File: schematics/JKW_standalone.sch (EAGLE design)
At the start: 225 parts, among them IC1 4093D, IC4 ATMEGA2560-16AU, Q1 BSS84, Q10 BSS84, Q11 BSS84, Q2 BSS84, Q3 BSS84, Q4 BSS84, Q5 BSS84, Q6 BSS84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

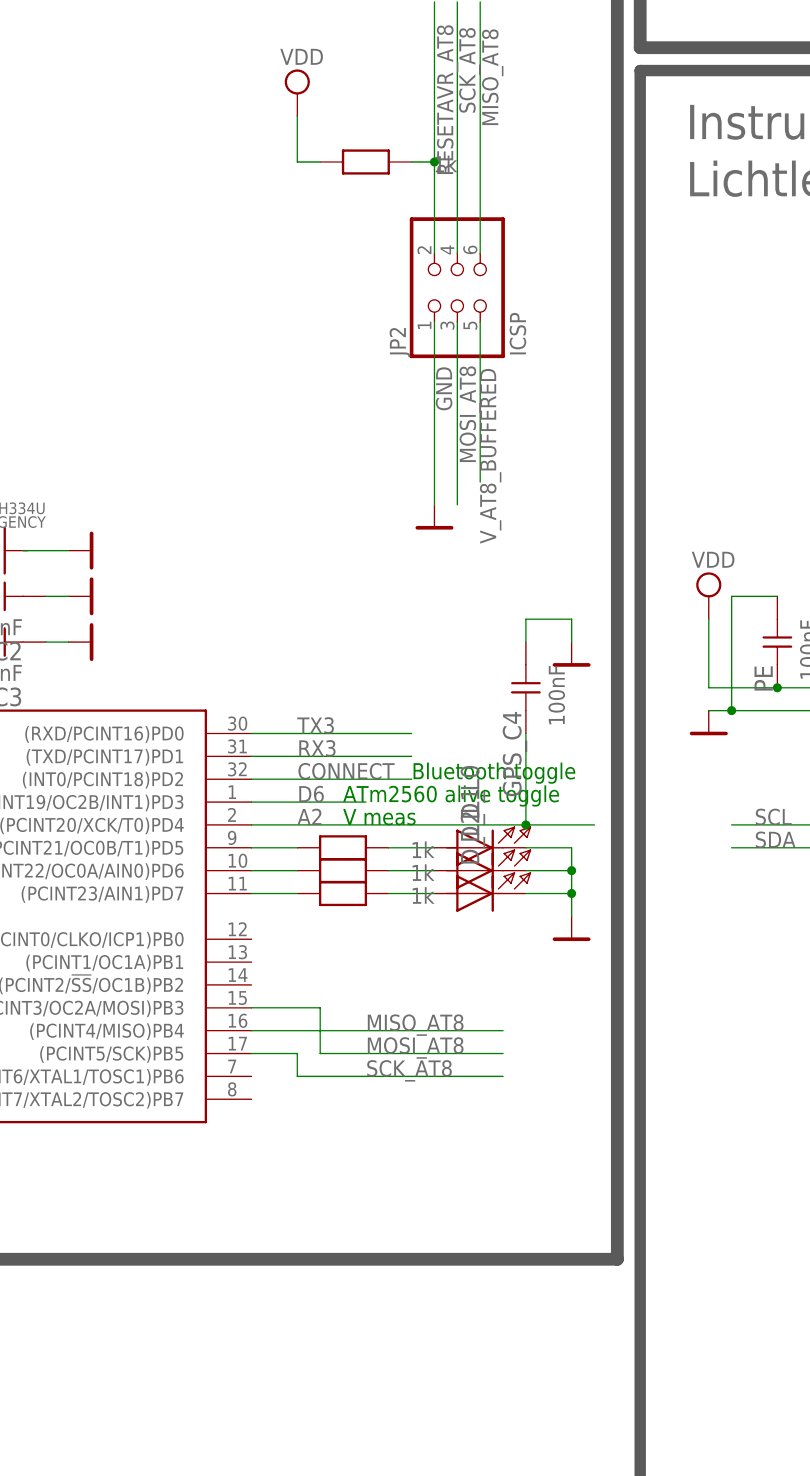
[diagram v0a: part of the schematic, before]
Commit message: Added second 16Mhz crystal
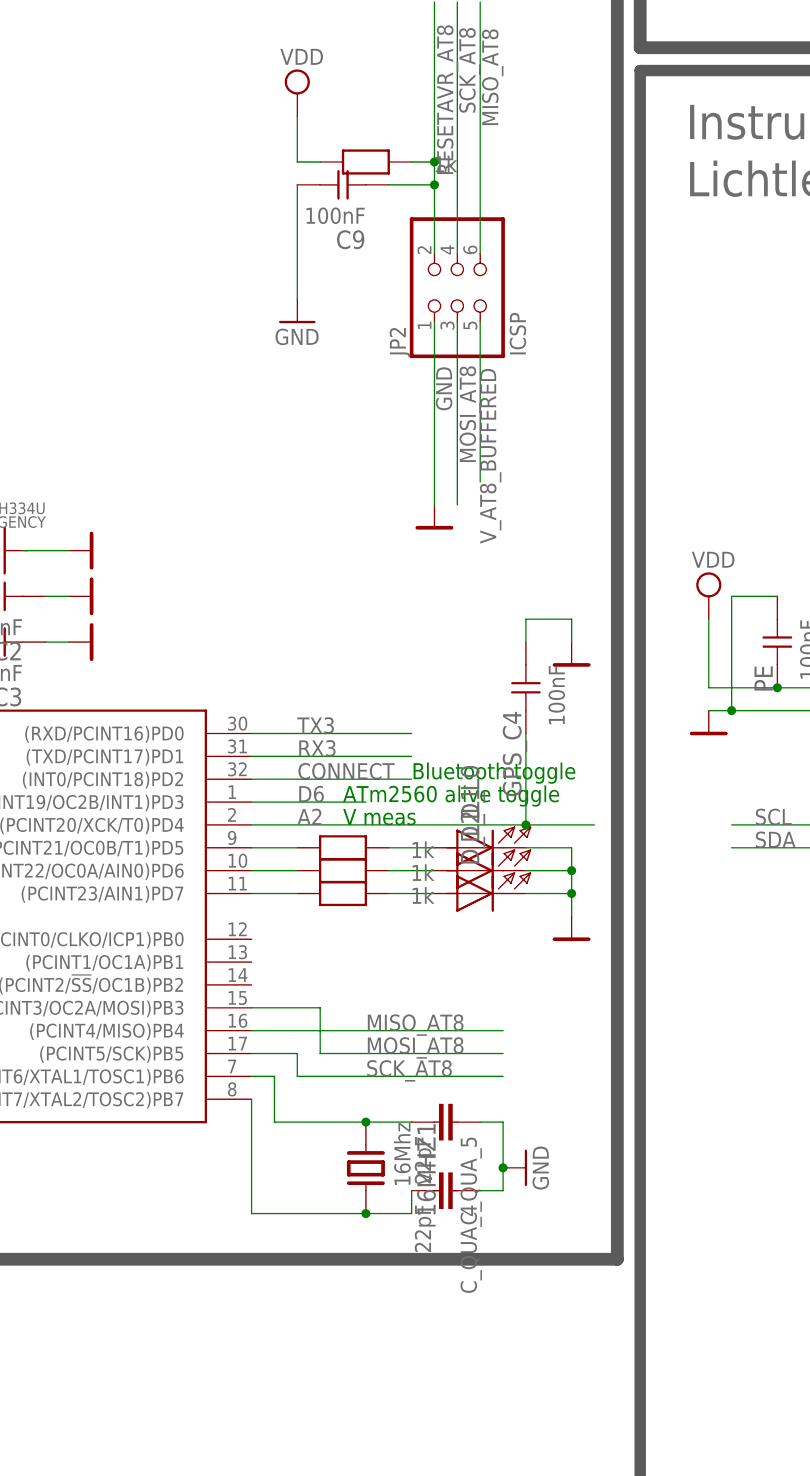
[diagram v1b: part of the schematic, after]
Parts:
- added 16MHZ1: 16Mhz, XT:XT-HC49-SMD
- added C9: 100nF, RCLDT:C0805
- added C_QUA_4, C_QUA_5: 22pF, rcl:C-EUC0805
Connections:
- new net N$63: 16MHZ1.1, C_QUA_5.2, U$1.(PCINT6/XTAL1/TOSC1)PB6
- new net N$65: 16MHZ1.2, C_QUA_4.2, U$1.(PCINT7/XTAL2/TOSC2)PB7
- net GND: now also C9.2, C_QUA_4.1, C_QUA_5.1
- net RESETAVR_AT8: now also C9.1
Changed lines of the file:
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@@
 <?xml version="1.0" encoding="utf-8"?>
 <!DOCTYPE eagle SYSTEM "eagle.dtd">
-<eagle version="6.1">
+<eagle version="6.2">
 <drawing>
 <settings>
@@
 <part name="SUPPLY22" library="supply2" deviceset="VDD" device=""/>
 <part name="U$1" library="Kolja" deviceset="ATMEGA328P-AU" device=""/>
+<part name="16MHZ1" library="XT" deviceset="XT" device="-HC49-SMD" value="16Mhz"/>
+<part name="C_QUA_4" library="rcl" deviceset="C-EU" device="C0805" value="22pF"/>
+<part name="C_QUA_5" library="rcl" deviceset="C-EU" device="C0805" value="22pF"/>
+<part name="GND37" library="SparkFun" deviceset="GND" device=""/>
+<part name="GND38" library="SparkFun" deviceset="GND" device=""/>
+<part name="C9" library="RCLDT" deviceset="C" device="0805" value="100nF"/>
 </parts>
 <sheets>
@@
 <instance part="SUPPLY22" gate="G$1" x="-149.86" y="60.96"/>
 <instance part="U$1" gate="G$1" x="-193.04" y="-7.62"/>
+<instance part="16MHZ1" gate="G$1" x="-142.24" y="-58.42" rot="R270"/>
+<instance part="C_QUA_4" gate="G$1" x="-132.08" y="-60.96" rot="R270"/>
+<instance part="C_QUA_5" gate="G$1" x="-132.08" y="-53.34" rot="R270"/>
+<instance part="GND37" gate="1" x="-124.46" y="-58.42" rot="R90"/>
+<instance part="GND38" gate="1" x="-149.86" y="35.56"/>
+<instance part="C9" gate="C" x="-144.78" y="50.8" rot="R180"/>
 </instances>
 <busses>
@@
 <junction x="-101.6" y="-7.62"/>
 </segment>
+<segment>
+<pinref part="C_QUA_5" gate="G$1" pin="1"/>
+<pinref part="GND37" gate="1" pin="GND"/>
+<wire x1="-129.54" y1="-53.34" x2="-127" y2="-53.34" width="0.1524" layer="91"/>
+<wire x1="-127" y1="-53.34" x2="-127" y2="-58.42" width="0.1524" layer="91"/>
+<pinref part="C_QUA_4" gate="G$1" pin="1"/>
+<wire x1="-127" y1="-58.42" x2="-127" y2="-60.96" width="0.1524" layer="91"/>
+<wire x1="-127" y1="-60.96" x2="-129.54" y2="-60.96" width="0.1524" layer="91"/>
+<junction x="-127" y="-58.42"/>
+</segment>
+<segment>
+<pinref part="GND38" gate="1" pin="GND"/>
+<pinref part="C9" gate="C" pin="2"/>
+<wire x1="-149.86" y1="50.8" x2="-149.86" y2="38.1" width="0.1524" layer="91"/>
+</segment>
 </net>
 <net name="DZ" class="0">
@@
 </segment>
 <segment>
-<wire x1="-134.62" y1="43.18" x2="-134.62" y2="53.34" width="0.1524" layer="91"/>
+<wire x1="-134.62" y1="43.18" x2="-134.62" y2="50.8" width="0.1524" layer="91"/>
 <label x="-134.3152" y="68.6816" size="1.778" layer="95" rot="R270"/>
 <pinref part="JP2" gate="A" pin="2"/>
 <pinref part="R_L3" gate="G$1" pin="2"/>
+<wire x1="-134.62" y1="50.8" x2="-134.62" y2="53.34" width="0.1524" layer="91"/>
 <wire x1="-134.62" y1="53.34" x2="-134.62" y2="71.12" width="0.1524" layer="91"/>
 <wire x1="-137.16" y1="53.34" x2="-134.62" y2="53.34" width="0.1524" layer="91"/>
 <junction x="-134.62" y="53.34"/>
+<wire x1="-134.62" y1="50.8" x2="-139.7" y2="50.8" width="0.1524" layer="91"/>
+<pinref part="C9" gate="C" pin="1"/>
+<junction x="-134.62" y="50.8"/>
 </segment>
 <segment>
@@
 </segment>
 </net>
+<net name="N$63" class="0">
+<segment>
+<pinref part="16MHZ1" gate="G$1" pin="1"/>
+<wire x1="-152.4" y1="-53.34" x2="-142.24" y2="-53.34" width="0.1524" layer="91"/>
+<pinref part="C_QUA_5" gate="G$1" pin="2"/>
+<wire x1="-142.24" y1="-53.34" x2="-137.16" y2="-53.34" width="0.1524" layer="91"/>
+<junction x="-142.24" y="-53.34"/>
+<pinref part="U$1" gate="G$1" pin="(PCINT6/XTAL1/TOSC1)PB6"/>
+<wire x1="-154.94" y1="-48.26" x2="-152.4" y2="-48.26" width="0.1524" layer="91"/>
+<wire x1="-152.4" y1="-48.26" x2="-152.4" y2="-53.34" width="0.1524" layer="91"/>
+</segment>
+</net>
+<net name="N$65" class="0">
+<segment>
+<pinref part="C_QUA_4" gate="G$1" pin="2"/>
+<wire x1="-137.16" y1="-60.96" x2="-137.16" y2="-63.5" width="0.1524" layer="91"/>
+<pinref part="16MHZ1" gate="G$1" pin="2"/>
+<wire x1="-137.16" y1="-63.5" x2="-142.24" y2="-63.5" width="0.1524" layer="91"/>
+<wire x1="-154.94" y1="-63.5" x2="-142.24" y2="-63.5" width="0.1524" layer="91"/>
+<junction x="-142.24" y="-63.5"/>
+<pinref part="U$1" gate="G$1" pin="(PCINT7/XTAL2/TOSC2)PB7"/>
+<wire x1="-154.94" y1="-50.8" x2="-154.94" y2="-63.5" width="0.1524" layer="91"/>
+</segment>
+</net>

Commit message: added pads for light sensor
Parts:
- removed D_P_EX_D2: 78-MMBZ5232B-V, diode:ZENER-DIODESOT23
- removed R_E0_0, R_E0_2, R_E0_4: n.b., RCLDT:R0805
- removed R_E0_1, R_E0_3: n.b. / 0R, RCLDT:R0805
- removed R_HB2: 600R, RCLDT:R0805
- added D12: 771-PMBD7000235, semicon-smd-ipc:D-A1-C3
- added D_VERPOL1: SS24T3G, RCLDT:D-SSMB-A+K
- added R_DEAKT_DAUER_P, R_DEAKT_DAUER_P1: 10k, RCLDT:R0805
- added T13: Mouser: 771-2N7002BK215 , N-Channel, 60V 350mA, SOT-23, 0,0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, RCLDT:T-P-FETBSS139
- added TX2: (no value), pinhead:PINHD-1X2
- added T_P_BRIDGE: PMV160UP215, Kolja:PMV160UP215
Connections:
- removed net D49: IC4.PL0(ICP4), R_E0_2.2, R_E0_4.2
- removed net N$24: 12V_F1.P$1, D_VERPOL.K
- removed net N$46: IC1B.O, R_E0_4.1
- removed net N$89: R_HB2.1, SPEEDOSTECKER.EX_IN_OUT_D2
- new net 12V_D_SAFE: 12V_F1.P$1, D_VERPOL.K, D_VERPOL1.K
- new net 12V_PERMANENT: R_DEAKT_DAUER_P.1, SPEEDOSTECKER.DAUER_VIN, T_P_BRIDGE.S
- new net SELF_PWR_UP: IC4.PL0(ICP4), R_DEAKT_DAUER_P1.1, T13.G
- net 12V: now also SPEEDOSTECKER.IGN_VIN; no longer SPEEDOSTECKER.VIN
- net A12: now also TX2.2
- net A13: now also TX2.1
- net B_LEFT: now also D12.C, R_DEAKT_DAUER_P.2, T13.D, T_P_BRIDGE.G; no longer IC4.PJ4(PCINT13)
- net GND: now also R_DEAKT_DAUER_P1.2, T13.S; no longer D_P_EX_D2.A, R_E0_3.1
- net N$41: now also D12.A, IC4.PJ4(PCINT13); no longer D_P_EX_D2.C, R_E0_1.1, R_HB2.2
- net N$45: now also D_VERPOL1.A, T_P_BRIDGE.D; no longer IC1B.I1, R_E0_0.1, R_E0_1.2, R_E0_2.1, R_E0_3.2
- net VDD: no longer IC1B.I0, R_E0_0.2
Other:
- note added: "there is a Diode at the Port to protect it against the 12V"
- note removed: "TODO: R hinzufügen?"
